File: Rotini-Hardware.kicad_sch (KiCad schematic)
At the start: 70 parts, among them J1 Conn_01x02, J2 Conn_01x02, J200 SH_PPM, J201 SH_LED, J202 SH_LED, Q20 AO3401A, Q50 SS8050, Q51 SS8050, U1 ESP32-S2, U2 Crystal_ESP32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

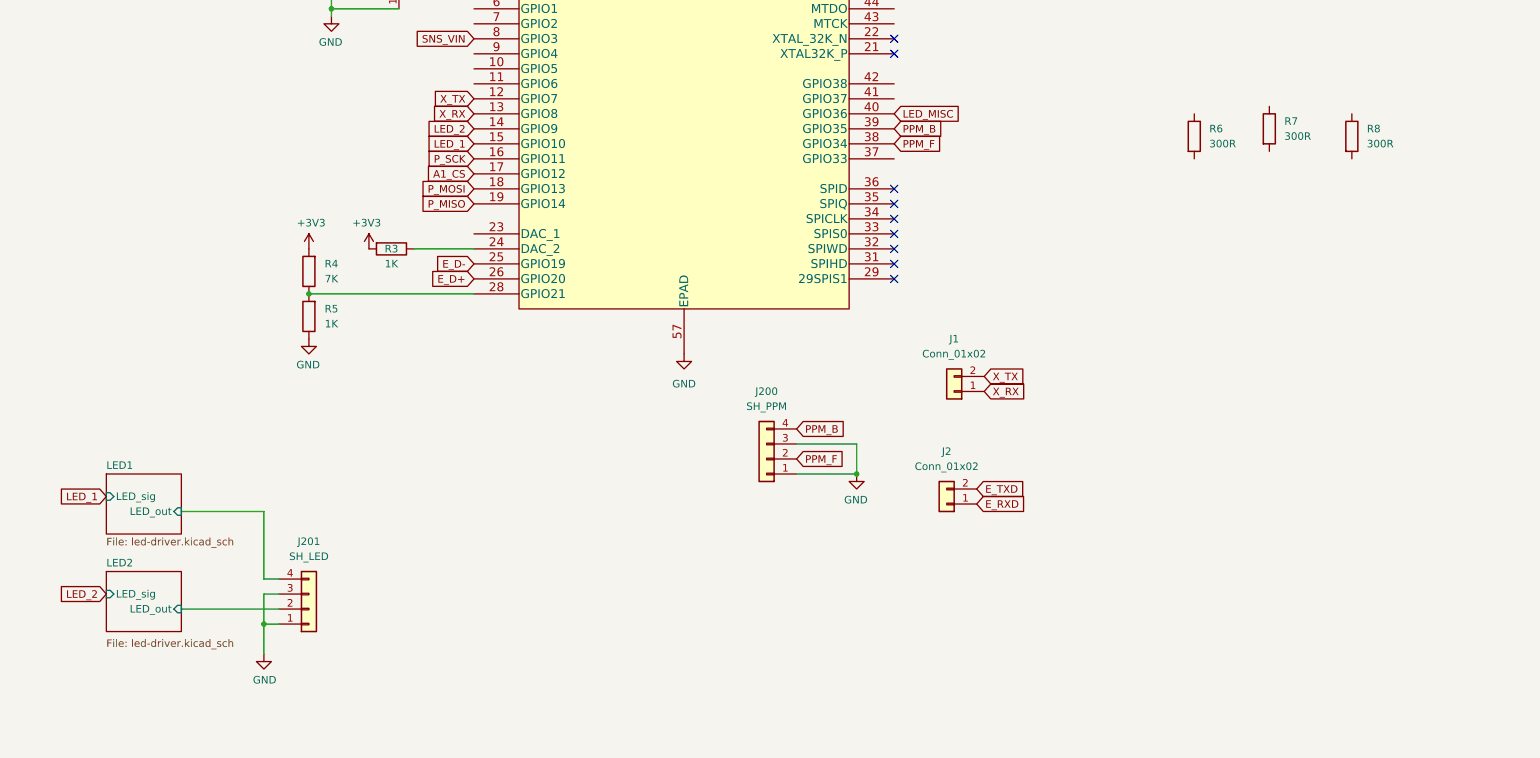
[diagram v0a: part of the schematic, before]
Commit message: Converted Project name to Rotini + files ordered for V1
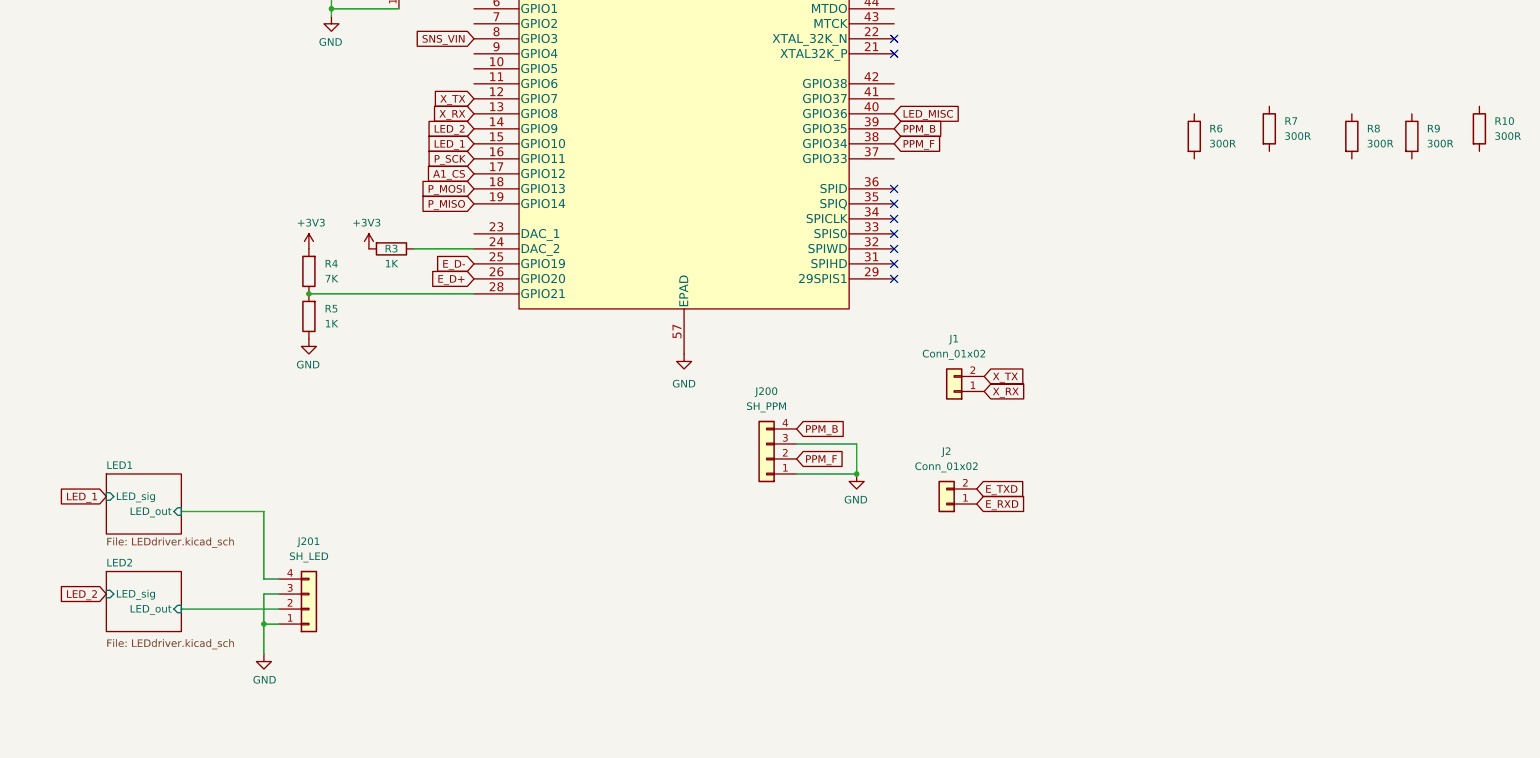
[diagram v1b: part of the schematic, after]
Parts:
- added R10, R9: 300R, Resistor_SMD:R_1206_3216Metric, symbol Device:R
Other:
- sheet LED1: file led-driver.kicad_sch -> LEDdriver.kicad_sch
- sheet LED2: file led-driver.kicad_sch -> LEDdriver.kicad_sch
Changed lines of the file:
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@@
+    (pin "2")
+  )
+  (symbol (lib_id "Device:R") (at 354.33 96.52 0) (unit 1)
+    (in_bom yes) (on_board yes) (fields_autoplaced)
+    (property "Reference" "R10" (id 0) (at 356.87 95.2499 0)
+      (effects (font (size 1.27 1.27)) (justify left))
+    )
+    (property "Value" "300R" (id 1) (at 356.87 97.7899 0)
+      (effects (font (size 1.27 1.27)) (justify left))
+    )
+    (property "Footprint" "Resistor_SMD:R_1206_3216Metric" (id 2) (at 352.552 96.52 90)
+      (effects (font (size 1.27 1.27)) hide)
+    )
+    (property "Datasheet" "https://lcsc.com/product-detail/Chip-Resistor---Surface-Mount_UNI-ROYALUniroyal-Elec-UNI-ROYALUniroyal-Elec-1206W4F3000T5E_C17887.html" (id 3) (at 354.33 96.52 0)
+      (effects (font (size 1.27 1.27)) hide)
+    )
+    (property "LCSC" "C17887" (id 4) (at 354.33 96.52 0)
+      (effects (font (size 1.27 1.27)) hide)
+    )
+    (pin "1")
     (pin "2")
   )
@@
     )
     (property "LCSC" "C25917" (id 4) (at 156.21 120.65 0)
+      (effects (font (size 1.27 1.27)) hide)
+    )
+    (pin "1")
+    (pin "2")
+  )
+  (symbol (lib_id "Device:R") (at 342.9 97.79 0) (unit 1)
+    (in_bom yes) (on_board yes) (fields_autoplaced)
+    (property "Reference" "R9" (id 0) (at 345.44 96.5199 0)
+      (effects (font (size 1.27 1.27)) (justify left))
+    )
+    (property "Value" "300R" (id 1) (at 345.44 99.0599 0)
+      (effects (font (size 1.27 1.27)) (justify left))
+    )
+    (property "Footprint" "Resistor_SMD:R_1206_3216Metric" (id 2) (at 341.122 97.79 90)
+      (effects (font (size 1.27 1.27)) hide)
+    )
+    (property "Datasheet" "https://lcsc.com/product-detail/Chip-Resistor---Surface-Mount_UNI-ROYALUniroyal-Elec-UNI-ROYALUniroyal-Elec-1206W4F3000T5E_C17887.html" (id 3) (at 342.9 97.79 0)
+      (effects (font (size 1.27 1.27)) hide)
+    )
+    (property "LCSC" "C17887" (id 4) (at 342.9 97.79 0)
       (effects (font (size 1.27 1.27)) hide)
     )
@@
       (effects (font (size 1.27 1.27)) (justify left bottom))
     )
-    (property "Sheet file" "led-driver.kicad_sch" (id 1) (at 121.92 165.6846 0)
+    (property "Sheet file" "LEDdriver.kicad_sch" (id 1) (at 121.92 165.6846 0)
       (effects (font (size 1.27 1.27)) (justify left top))
     )
@@
       (effects (font (size 1.27 1.27)) (justify left bottom))
     )
-    (property "Sheet file" "led-driver.kicad_sch" (id 1) (at 121.92 182.88 0)
+    (property "Sheet file" "LEDdriver.kicad_sch" (id 1) (at 121.92 182.88 0)
       (effects (font (size 1.27 1.27)) (justify left top))
     )
@@
       (reference "#PWR0120") (unit 1) (value "+3V3") (footprint "")
     )
+    (path "/8a42e13d-ed03-4053-bea9-6b241e81b50a/3eaf3c33-8162-4d3c-87c0-f763cf970812"
+      (reference "#PWR0121") (unit 1) (value "GND") (footprint "")
+    )
+    (path "/8a42e13d-ed03-4053-bea9-6b241e81b50a/aa1bffdd-ea1d-4626-bc96-3bed0a131e6e"
+      (reference "#PWR0122") (unit 1) (value "VCC") (footprint "")
+    )
     (path "/72bba200-e8f0-4176-acbf-4460b61b53f8/ca1156f9-ac05-417f-8685-fd679d5978ff"
       (reference "#PWR0123") (unit 1) (value "GND") (footprint "")
@@
       (reference "#PWR0151") (unit 1) (value "GND") (footprint "")
     )
+    (path "/8a42e13d-ed03-4053-bea9-6b241e81b50a/0f1fde14-8b31-4490-880f-131294de258e"
+      (reference "#PWR0152") (unit 1) (value "VCC") (footprint "")
+    )
     (path "/a89000bb-1907-4e2d-9ff9-7ce784d5f34f"
       (reference "#PWR0153") (unit 1) (value "GND") (footprint "")
@@
       (reference "#PWR0172") (unit 1) (value "+3V3") (footprint "")
     )
-    (path "/8a42e13d-ed03-4053-bea9-6b241e81b50a/3eaf3c33-8162-4d3c-87c0-f763cf970812"
-      (reference "#PWR0174") (unit 1) (value "GND") (footprint "")
-    )
-    (path "/8a42e13d-ed03-4053-bea9-6b241e81b50a/0f1fde14-8b31-4490-880f-131294de258e"
+    (path "/c8ae6305-850c-49e4-9b5b-36e9c53035a5/3eaf3c33-8162-4d3c-87c0-f763cf970812"
+      (reference "#PWR0173") (unit 1) (value "GND") (footprint "")
+    )
+    (path "/c8ae6305-850c-49e4-9b5b-36e9c53035a5/aa1bffdd-ea1d-4626-bc96-3bed0a131e6e"
+      (reference "#PWR0174") (unit 1) (value "VCC") (footprint "")
+    )
+    (path "/c8ae6305-850c-49e4-9b5b-36e9c53035a5/0f1fde14-8b31-4490-880f-131294de258e"
       (reference "#PWR0175") (unit 1) (value "VCC") (footprint "")
-    )
-    (path "/8a42e13d-ed03-4053-bea9-6b241e81b50a/aa1bffdd-ea1d-4626-bc96-3bed0a131e6e"
-      (reference "#PWR0176") (unit 1) (value "VCC") (footprint "")
-    )
-    (path "/c8ae6305-850c-49e4-9b5b-36e9c53035a5/3eaf3c33-8162-4d3c-87c0-f763cf970812"
-      (reference "#PWR0178") (unit 1) (value "GND") (footprint "")
-    )
-    (path "/c8ae6305-850c-49e4-9b5b-36e9c53035a5/0f1fde14-8b31-4490-880f-131294de258e"
-      (reference "#PWR0179") (unit 1) (value "VCC") (footprint "")
-    )
-    (path "/c8ae6305-850c-49e4-9b5b-36e9c53035a5/aa1bffdd-ea1d-4626-bc96-3bed0a131e6e"
-      (reference "#PWR0180") (unit 1) (value "VCC") (footprint "")
     )
     (path "/480c93b5-1e2d-48fd-b6f0-fd2577953d3b"
@@
     )
     (path "/8a42e13d-ed03-4053-bea9-6b241e81b50a/55983554-e3a8-44a4-b83f-db8b831863cf"
-      (reference "Q30") (unit 1) (value "LBSS84LT1G") (footprint "Package_TO_SOT_SMD:SOT-23")
+      (reference "Q30") (unit 1) (value "LBSS84LT1G") (footprint "")
     )
     (path "/8a42e13d-ed03-4053-bea9-6b241e81b50a/11a51356-ce36-4ff7-a926-138e30773d2d"
-      (reference "Q31") (unit 1) (value "2N7002") (footprint "Package_TO_SOT_SMD:SOT-23")
+      (reference "Q31") (unit 1) (value "2N7002") (footprint "")
     )
     (path "/c8ae6305-850c-49e4-9b5b-36e9c53035a5/55983554-e3a8-44a4-b83f-db8b831863cf"
-      (reference "Q32") (unit 1) (value "LBSS84LT1G") (footprint "Package_TO_SOT_SMD:SOT-23")
+      (reference "Q32") (unit 1) (value "LBSS84LT1G") (footprint "")
     )
     (path "/c8ae6305-850c-49e4-9b5b-36e9c53035a5/11a51356-ce36-4ff7-a926-138e30773d2d"
-      (reference "Q33") (unit 1) (value "2N7002") (footprint "Package_TO_SOT_SMD:SOT-23")
+      (reference "Q33") (unit 1) (value "2N7002") (footprint "")
     )
     (path "/d07c99eb-5efc-4444-8984-2a3c626d9070"
@@
       (reference "R8") (unit 1) (value "300R") (footprint "Resistor_SMD:R_1206_3216Metric")
     )
+    (path "/b35acdd3-22b7-47af-aeab-f5c405857bcd"
+      (reference "R9") (unit 1) (value "300R") (footprint "Resistor_SMD:R_1206_3216Metric")
+    )
+    (path "/48b8fc14-5e34-44c3-9bf1-d395048f19c1"
+      (reference "R10") (unit 1) (value "300R") (footprint "Resistor_SMD:R_1206_3216Metric")
+    )
     (path "/00000000-0000-0000-0000-000060dcbf0d"
       (reference "R20") (unit 1) (value "68K") (footprint "Resistor_SMD:R_0402_1005Metric")
@@
     )
     (path "/8a42e13d-ed03-4053-bea9-6b241e81b50a/917f93d3-e40c-47ba-a7ea-45bfa808d248"
-      (reference "R30") (unit 1) (value "10K") (footprint "Resistor_SMD:R_0402_1005Metric")
+      (reference "R30") (unit 1) (value "10K") (footprint "")
     )
     (path "/8a42e13d-ed03-4053-bea9-6b241e81b50a/34d30913-86c1-470f-ba69-fd67e11fe553"
-      (reference "R31") (unit 1) (value "10K") (footprint "Resistor_SMD:R_0402_1005Metric")
+      (reference "R31") (unit 1) (value "10K") (footprint "")
     )
     (path "/8a42e13d-ed03-4053-bea9-6b241e81b50a/92b8b94b-b181-45e7-8ce3-358e9c0d972c"
-      (reference "R32") (unit 1) (value "1K") (footprint "Resistor_SMD:R_0402_1005Metric")
+      (reference "R32") (unit 1) (value "1K") (footprint "")
     )
     (path "/c8ae6305-850c-49e4-9b5b-36e9c53035a5/917f93d3-e40c-47ba-a7ea-45bfa808d248"
-      (reference "R33") (unit 1) (value "10K") (footprint "Resistor_SMD:R_0402_1005Metric")
+      (reference "R33") (unit 1) (value "10K") (footprint "")
     )
     (path "/c8ae6305-850c-49e4-9b5b-36e9c53035a5/34d30913-86c1-470f-ba69-fd67e11fe553"
-      (reference "R34") (unit 1) (value "10K") (footprint "Resistor_SMD:R_0402_1005Metric")
+      (reference "R34") (unit 1) (value "10K") (footprint "")
     )
     (path "/c8ae6305-850c-49e4-9b5b-36e9c53035a5/92b8b94b-b181-45e7-8ce3-358e9c0d972c"
-      (reference "R36") (unit 1) (value "1K") (footprint "Resistor_SMD:R_0402_1005Metric")
+      (reference "R35") (unit 1) (value "1K") (footprint "")
     )
     (path "/973929e4-3414-4422-ad3d-156b47b18ecc"

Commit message: First push with Rotini V2 features, removed CP210x USB circuit
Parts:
- removed C50, C51: 100nF, Capacitor_SMD:C_0402_1005Metric, symbol Device:C_Small
- removed C52: 10uF, Capacitor_SMD:C_0402_1005Metric, symbol Device:C_Small
- removed Q50, Q51: SS8050, Package_TO_SOT_SMD:SOT-23, symbol Device:Q_NPN_BEC
- removed R10, R6, R7, R8, R9: 300R, Resistor_SMD:R_1206_3216Metric, symbol Device:R
- removed R50, R51, R52, R53: 1K, Resistor_SMD:R_0402_1005Metric, symbol Device:R
- removed R54, R55: 5.1K, Resistor_SMD:R_0402_1005Metric, symbol Device:R
- removed U50: CP2102-GMR, Package_DFN_QFN:QFN-28-1EP_5x5mm_P0.5mm_EP3.35x3.35mm, symbol AlfredoSymbols:CP2102-GMR
- removed U51: USB_C_Receptacle, AlfredoFootprints:USB_TYPE-C-31-M-12, symbol Connector:USB_C_Receptacle
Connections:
- no-connect marks 41 -> 25
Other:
- note added: "TODO: Change via size to avoid fee! remove redundant parts ESP8285 wifi antenna? FIX 12KRES provide pin breakouts incase jst sh is bad fix TCXO -> XO option to provide 3.3v to leds? use differet SH sizes (or one big one?) screw holes Done: SR/SZ -> 1mm JST SH What programming interface/connector? how to do LEDs? support 6s (26V) "stiff" 1K pull resistors mando for RF resilance smaller XOs reverse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"
- note removed: "TODO: By H3LIS accelerometers Order H3LIS accelerometers for global parts storage Eventual: remove redundant parts ESP8285 wifi antenna? Done: SR/SZ -> 1mm JST SH What programming interface/connector? how to do LEDs? support 6s (26V) "stiff" 1K pull resistors mando for RF resilance smaller XOs reverse polarity protection? route board Select all JLC components"
- note removed: "what mcu? (clk speed/upload ease/arduino/JLC) STM32 (use STM32 with mircousb for prog/debug, use boot button to prog) ESP32 Atmega328 RP2040 mega328U4 picked ESP32"
- moved on the sheet: R56, R57, U52

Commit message: fixed 26MHz XO and 12KRES resistor
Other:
- note added: "TODO: Change via size to avoid fee! remove redundant parts ESP8285 wifi antenna? provide pin breakouts incase jst sh is bad option to provide 3.3v to leds? use differet SH sizes (or one big one?) screw holes improve jumpers Done: SR/SZ -> 1mm JST SH What programming interface/connector? how to do LEDs? support 6s (26V) "stiff" 1K pull resistors mando for RF resilance smaller XOs reverse polarity 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"
- note removed: "TODO: Change via size to avoid fee! remove redundant parts ESP8285 wifi antenna? FIX 12KRES provide pin breakouts incase jst sh is bad fix TCXO -> XO option to provide 3.3v to leds? use differet SH sizes (or one big one?) screw holes Done: SR/SZ -> 1mm JST SH What programming interface/connector? how to do LEDs? support 6s (26V) "stiff" 1K pull resistors mando for RF resilance smaller XOs reverse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"
- moved on the sheet: R56, R57, U52

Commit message: Hardware bought of Rotini V2
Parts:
- removed J1, J2: Conn_01x02, Connector_PinHeader_2.54mm:PinHeader_1x02_P2.54mm_Vertical, symbol Connector_Generic:Conn_01x02
- removed J200: SH_PPM, Connector_JST:JST_SH_SM04B-SRSS-TB_1x04-1MP_P1.00mm_Horizontal, symbol Connector_Generic:Conn_01x04
- removed J202: SH_LED, Connector_JST:JST_SH_SM04B-SRSS-TB_1x04-1MP_P1.00mm_Horizontal, symbol Connector_Generic:Conn_01x04
- removed R2: 500R, Resistor_SMD:R_0402_1005Metric, symbol Device:R
- added J202: SH_POW, Connector_JST:JST_SH_SM02B-SRSS-TB_1x02-1MP_P1.00mm_Horizontal, symbol Connector_Generic:Conn_01x02
- added J203: SH_PPM, Connector_JST:JST_SH_SM03B-SRSS-TB_1x03-1MP_P1.00mm_Horizontal, symbol Connector_Generic:Conn_01x03
- added J205: VIN, AlfredoFootprints:TGD-antenna-THT, symbol Connector_Generic:Conn_01x01
- added J206: GND, AlfredoFootprints:TGD-antenna-THT, symbol Connector_Generic:Conn_01x01
- added J207: FOO, AlfredoFootprints:TGD-antenna-THT, symbol Connector_Generic:Conn_01x01
- added J208: BAR, AlfredoFootprints:TGD-antenna-THT, symbol Connector_Generic:Conn_01x01
- added TP1, TP3: ELRS_TX, AlfredoFootprints:PogoPad1, symbol Connector:TestPoint
- added TP2: ELRS_RX, AlfredoFootprints:PogoPad1, symbol Connector:TestPoint
- R4: value 7K -> 3.3K; LCSC C25917 -> C25890
- renumbered J201 to J204
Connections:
- net GND: now also J202.1 (Pin_1), J203.1 (Pin_1), J206.1 (Pin_1), TP3.1
- net PPM_B: now also J203.3 (Pin_3), J208.1 (Pin_1)
- net PPM_F: now also J203.2 (Pin_2), J207.1 (Pin_1)
- net X_RX: now also TP2.1
- net X_TX: now also TP1.1
- net at Q20.3 (D): now also J202.2 (Pin_2), J205.1 (Pin_1)
- net SNS_VER: now reaches R4.1, R5.2
- net SNS_VER: now also U1.10 (GPIO5); no longer U1.28 (GPIO21)
- net E_RXD: no longer names the net of U1.49 (U0RXD)
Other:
- note added: "TODO: option to provide 3.3v to leds? TVS Diodes hookup accel int pins add SH pin for curr sns Done: SR/SZ -> 1mm JST SH What programming interface/connector? how to do LEDs? support 6s (26V) "stiff" 1K pull resistors mando for RF resilance smaller XOs reverse polarity protection? route board Select all JLC components Order H3LIS accelerometers for global parts storage fix TCXO -> XO FIX 12KRES c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"
- note added: "V1: 7K/1K -> 0.125*3.3 V2: 3K/1K -> 0.250*3.3 V3: 5K/3K -> 0.375*3.3 V4: 1K/1K -> 0.500*3.3"
- note removed: "TODO: Change via size to avoid fee! remove redundant parts ESP8285 wifi antenna? provide pin breakouts incase jst sh is bad option to provide 3.3v to leds? use differet SH sizes (or one big one?) screw holes improve jumpers Done: SR/SZ -> 1mm JST SH What programming interface/connector? how to do LEDs? support 6s (26V) "stiff" 1K pull resistors mando for RF resilance smaller XOs reverse polarity 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"
- moved on the sheet: D21, J204, Q20, R22, R56, R57, U52

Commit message: Cleaned up schematic
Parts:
- TP3: value ELRS_TX -> ELRS_GND
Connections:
- net GND: now also R56.2; no longer R56.1
- net at U52.A5 (CC1): now also R56.1; no longer R56.2
- net VBUS: no longer names the net of D20.2 (A), U52.A4 (VBUS), U52.A9 (VBUS), U52.B4 (VBUS), U52.B9 (VBUS)
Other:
- note added: "Analog Sensing"
- note added: "Digital"
- note added: "LEDs"
- note added: "Main MCU"
- note added: "Power"
- note added: "Signal Out"
- note added: "USB"
- note added: "V1: SNS_VER reads 0V V2: 3K/1K -> 0.250*3.3V V3: 5K/3K -> 0.375*3.3V V4: 1K/1K -> 0.500*3.3V"
- note removed: "1-19 E - ESP32-S2 20-29 3.3V regulator 30-49 LEDs/sensing/Accelerometer 50-59 USB 60-89 X - ExpressLRS"
- note removed: "TODO: option to provide 3.3v to leds? TVS Diodes hookup accel int pins add SH pin for curr sns Done: SR/SZ -> 1mm JST SH What programming interface/connector? how to do LEDs? support 6s (26V) "stiff" 1K pull resistors mando for RF resilance smaller XOs reverse polarity protection? route board Select all JLC components Order H3LIS accelerometers for global parts storage fix TCXO -> XO FIX 12KRES c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"
- note removed: "V1: 7K/1K -> 0.125*3.3 V2: 3K/1K -> 0.250*3.3 V3: 5K/3K -> 0.375*3.3 V4: 1K/1K -> 0.500*3.3"
- note removed: "https://www.espressif.com/sites/default/files/documentation/esp32-s2_hardware_design_guidelines_en.pdf"
- title: spin-tgd-control -> Rotini V2
- moved on the sheet: C1, C10, C11, C12, C13, C14, C2, C20, C21, C22, C23, C3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
